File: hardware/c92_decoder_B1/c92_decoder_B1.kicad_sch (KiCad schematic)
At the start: 83 parts, among them J1 TRACK_1, J10 F2_OUT, J11 F3_OUT, J12 F4_OUT, J13 GND, J14 CAP, J2 SWD, J3 TRACK_2, J4 F0F_OUT, J5 F0R_OUT, J6 MOTOR_L, J7 MOTOR_R, J8 VDD, J9 F1_OUT, Q1 DMC3071LVT, Q2 DMC3071LVT, Q3 DDC114YU, Q4 DDC114YU, Q5 DMN3190LDW, Q6 DMN3190LDW, Q7 DMN3190LDW, SW1 ADDRESS, U1 TPS70933DBVR, U2 STM32G031G8U6, U3 INA180A3

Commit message: started B1 hardware
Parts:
- removed C14, C15, C16: 100n, Slonket_Footprints:C_0402, symbol Device:C
- removed Q1, Q2: DMC3071LVT, Slonket_Footprints:U_SOT-23-6, symbol Transistor_FET:DMC3071LVT
- removed Q3: DDC114YU, Slonket_Footprints:U_SOT-363, symbol Transistor_BJT:Q_Dual_NPN_NPN_BRT_E1B1C2E2B2C1
- removed unit 1 of Q4
- removed R10, R11, R17: 47k, Slonket_Footprints:R_0402, symbol Device:R
- removed R12, R13, R14: 10k, Slonket_Footprints:R_0402, symbol Device:R
- removed R15: 5k1, Slonket_Footprints:R_0402, symbol Device:R
- removed R16: 20m, Slonket_Footprints:R_0603, symbol Device:R
- removed R4, R5, R6, R7, R8, R9: 1k, Slonket_Footprints:R_0402, symbol Device:R
- removed U3: INA180A3, Slonket_Footprints:U_SOT-23-5, symbol Amplifier_Current:INA180A2
- added C? (x6): 22n, Slonket_Footprints:C_0402, symbol Device:C
- added C? (x2): 10u, Slonket_Footprints:C_1206, symbol Device:C
- added C? (x2): 100n, Slonket_Footprints:C_0402, symbol Device:C
- added C? (x2): 100n, Slonket_Footprints:C_0603, symbol Device:C
- added R? (x12): 10k, Slonket_Footprints:R_0402, symbol Device:R
- added R? (x4): 4k7, Slonket_Footprints:R_0402, symbol Device:R
- added R? (x4): 47k, Slonket_Footprints:R_0402, symbol Device:R
- added U?: DRV8876RGTR, Slonket_Footprints:U_TI_VQFN-16_3.1x3.1_P0.5_EP1, symbol Slonket_Symbols:DRV8876RGTR
- added U?: DRV8231ADSG, Package_SON:WSON-8-1EP_2x2mm_P0.5mm_EP0.9x1.6mm, symbol Driver_Motor:DRV8231ADSG
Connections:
- net +3V3: now also R?.2, R?.2, R?.2, R?.2, R?.2, R?.2, U?.14 (PMODE), U?.3 (VREF), U?.4 (VREF)
- net GND: now also C?.2, C?.2, C?.2, C?.2, C?.2, C?.2, C?.2, C?.2, C?.2, C?.2, R?.1, R?.1, R?.1, R?.1, R?.1, R?.1, U?.13 (GND), U?.17 (EP), U?.7 (GND), U?.7 (PGND), U?.9 (GND)
- net MOTOR_R: now also R?.1, R?.1, U?.8 (OUT2), U?.8 (OUT2)
- net VDD: now also C?.1, C?.1, C?.1, C?.1, C?.1, U?.5 (VM), U?.9 (VM)
- net BRIDGE_L: no longer names the net of U2.23 (PB3)
- net BRIDGE_R: no longer names the net of U2.24 (PB4)
- net M_BEMF: no longer names the net of U2.27 (PB7)
- net M_PWM: no longer names the net of U2.22 (PA15)
- net V_PROP_I: no longer names the net of U2.11 (PA5)
- new net: C?.1, R?.1, R?.1, R?.2, R?.2 (x4)
- new net: R?.1, U?.1 (~{SLEEP})
- new net: C?.2, U?.10 (VCP)
- new net: C?.1, U?.11 (CPH)
- new net: C?.2, U?.12 (CPL)
- new net BEMF_F: R?.2, R?.2
- new net BEMF_R: R?.2, R?.2
- new net MOTOR_F: R?.1, R?.1, U?.6 (OUT1), U?.6 (OUT1)
- new net PWM_F: U?.15 (IN1), U?.3 (IN1)
- new net PWM_R: U?.16 (IN2), U?.2 (IN2)
- new net VPROPI: C?.1, C?.1, R?.2, R?.2, U?.1 (IPROPI), U?.4 (IPROPI)
- new net ~{FAULT}: R?.1, U?.2 (~{FAULT})
- no-connect marks 1 -> 2
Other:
- note removed: "BEMF SENSING"
- note removed: "CURRENT SENSING"
- note removed: "Gain = 2V/A"
- note removed: "Output is approx 1/4"
- moved on the sheet: C10, C11, C12, C13

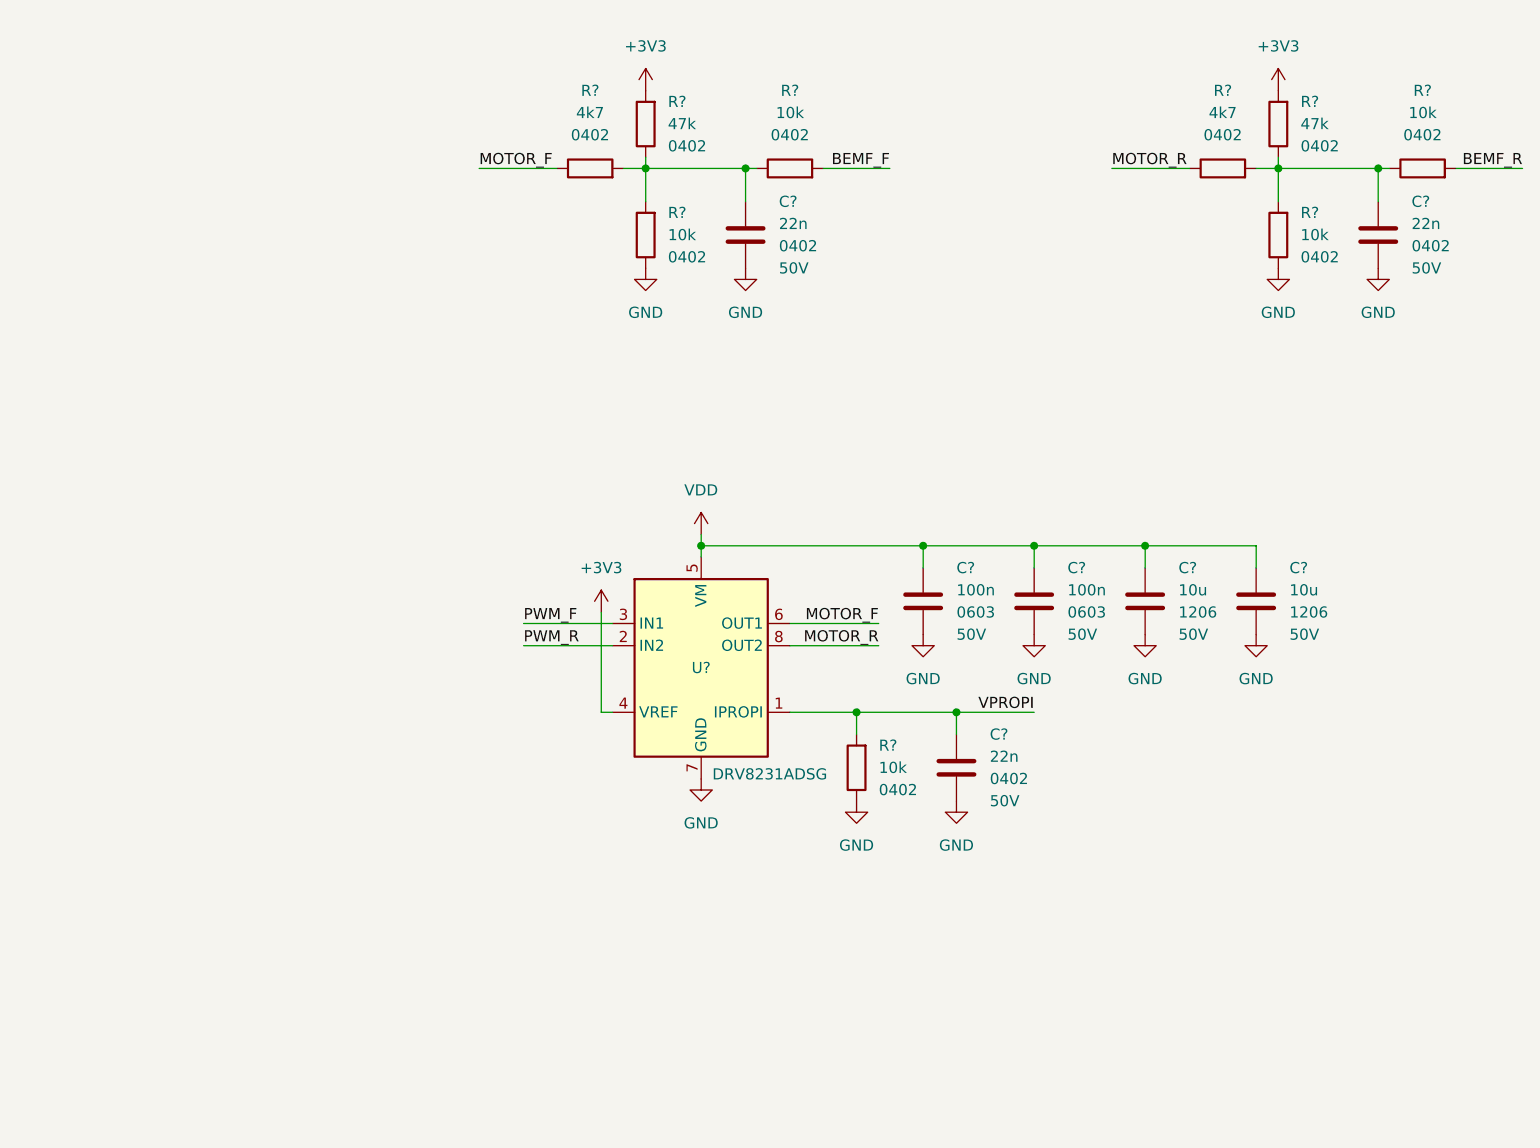
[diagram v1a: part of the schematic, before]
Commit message: made c92 core; modular decoder layout
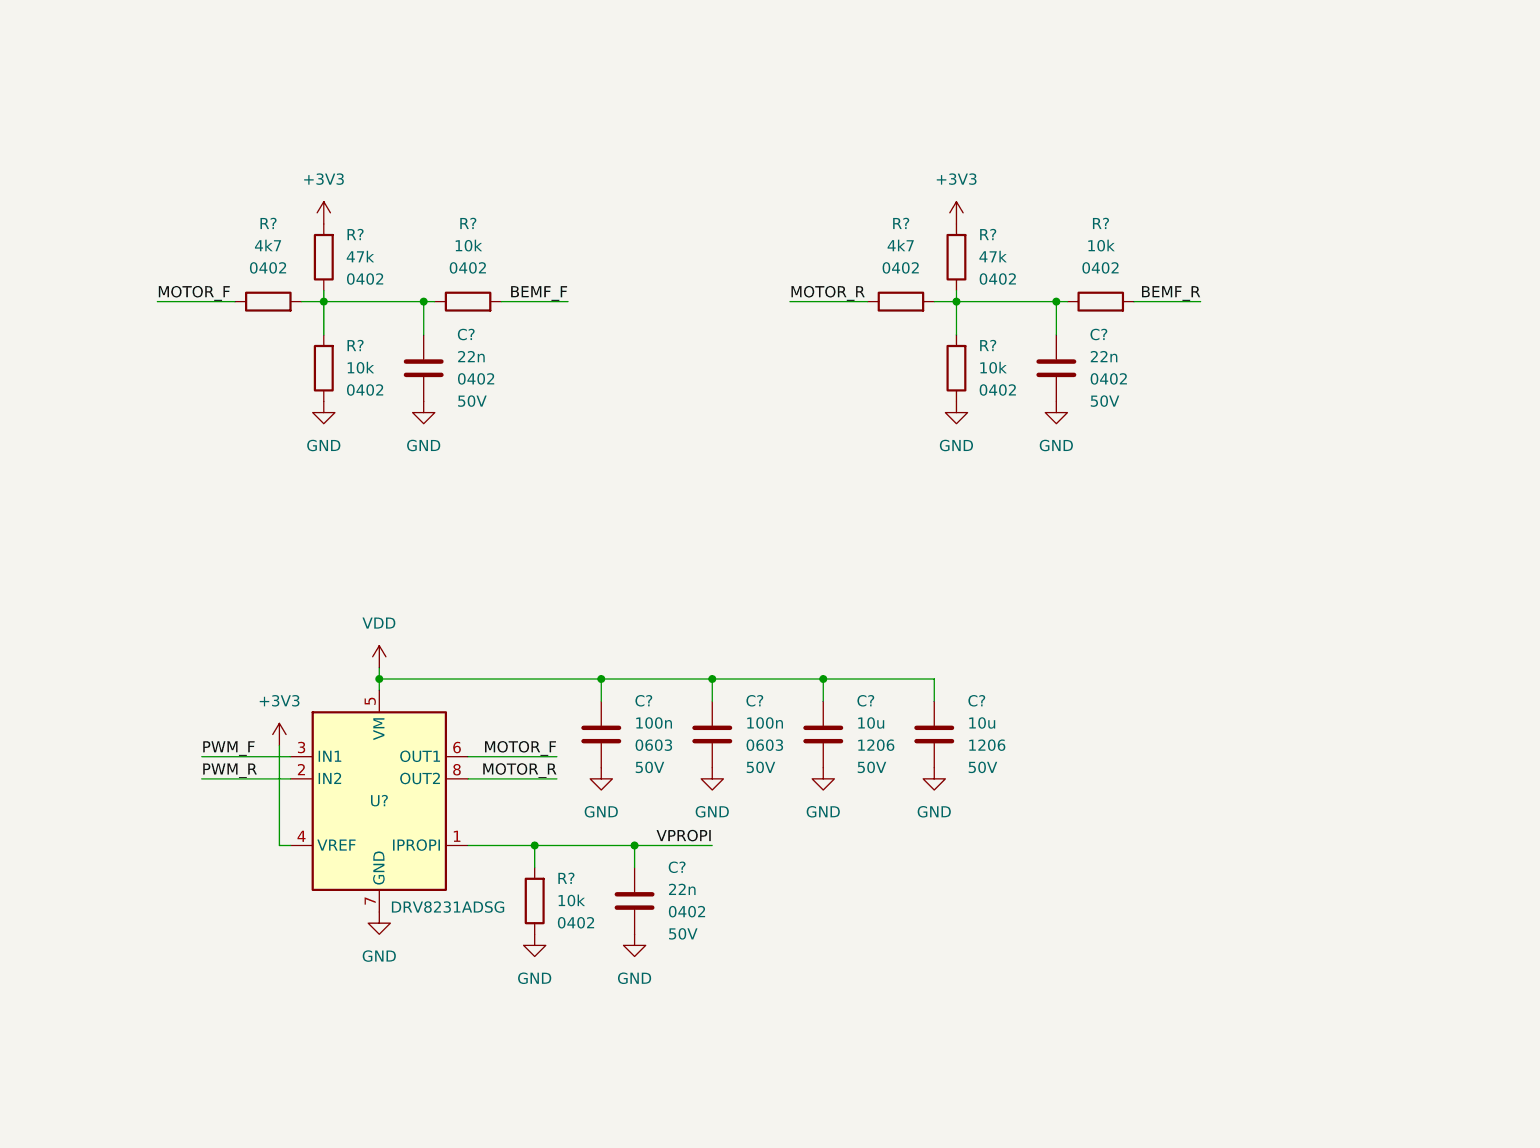
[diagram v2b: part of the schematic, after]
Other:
- moved on the sheet: C?, R?, U?
